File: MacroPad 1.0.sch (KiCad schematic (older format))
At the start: 10 parts

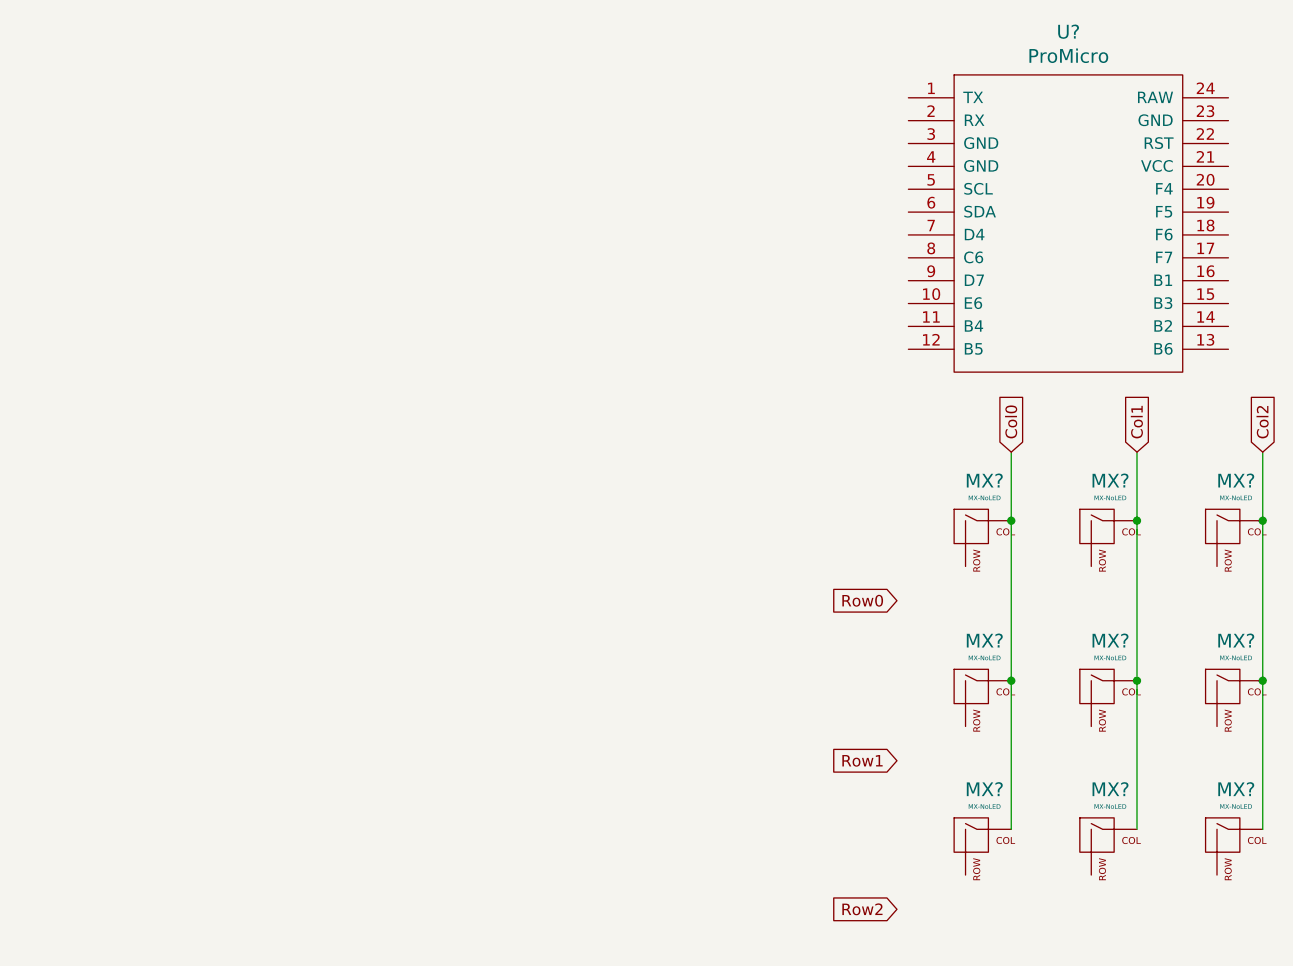
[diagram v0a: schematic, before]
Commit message: Completed Main Schematic
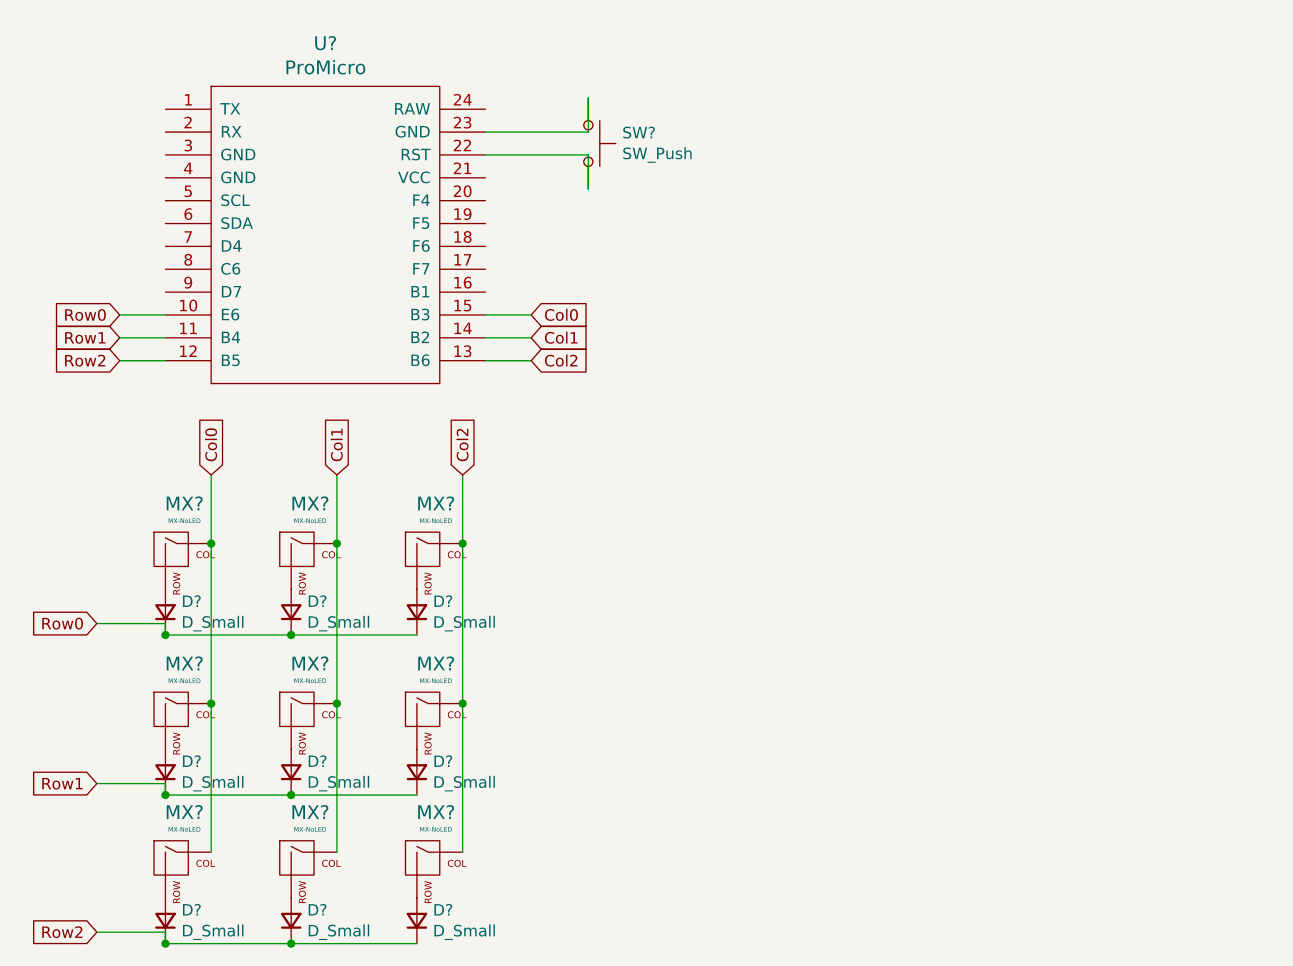
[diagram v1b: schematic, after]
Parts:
- added D? (x9): D_Small, symbol Device:D_Small
- added SW?: SW_Push, symbol Switch:SW_Push
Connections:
- net Col0: now also U?.15 (B3)
- net Col1: now also U?.14 (B2)
- net Col2: now also U?.13 (B6)
- net Row0: now also U?.10 (E6), D?.1 (K), D?.1 (K), D?.1 (K)
- net Row1: now also U?.11 (B4), D?.1 (K), D?.1 (K), D?.1 (K)
- net Row2: now also U?.12 (B5), D?.1 (K), D?.1 (K), D?.1 (K)
- net at U?.22 (RST): now also SW?.2
- net at U?.23 (GND): now also SW?.1
- net at MX?.2 (ROW): now also D?.2 (A) (x9)
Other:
- moved on the sheet: MX?, U?
